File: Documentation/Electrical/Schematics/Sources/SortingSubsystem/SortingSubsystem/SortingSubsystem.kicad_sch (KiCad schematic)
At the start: 5 parts

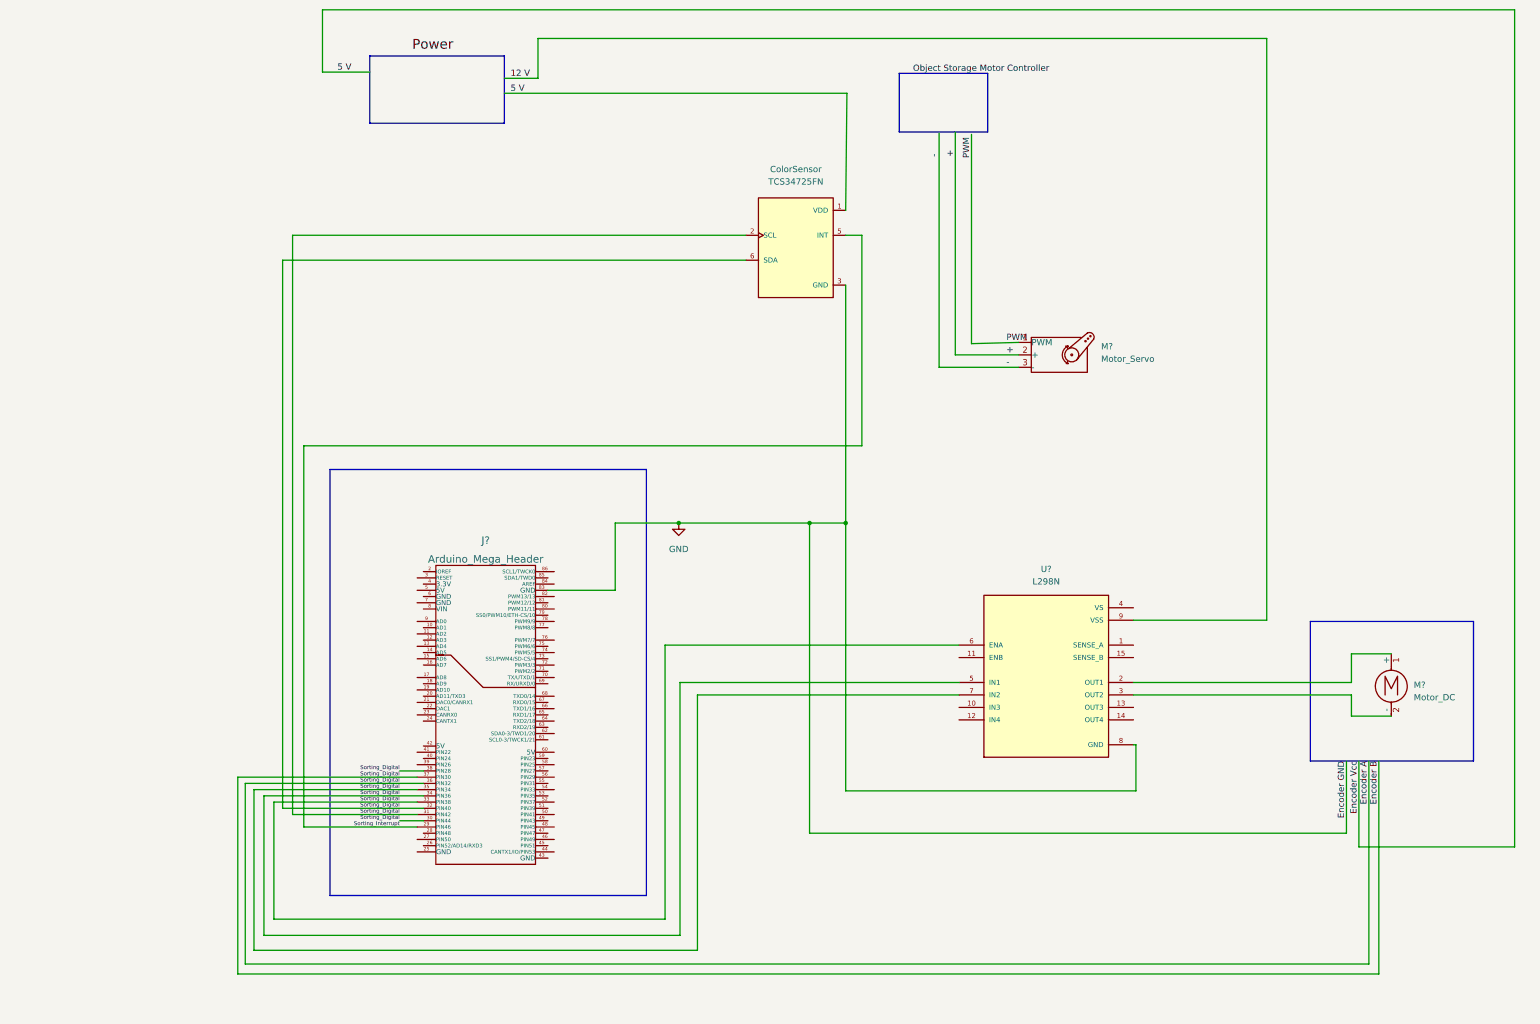
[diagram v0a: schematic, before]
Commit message: added schematic file
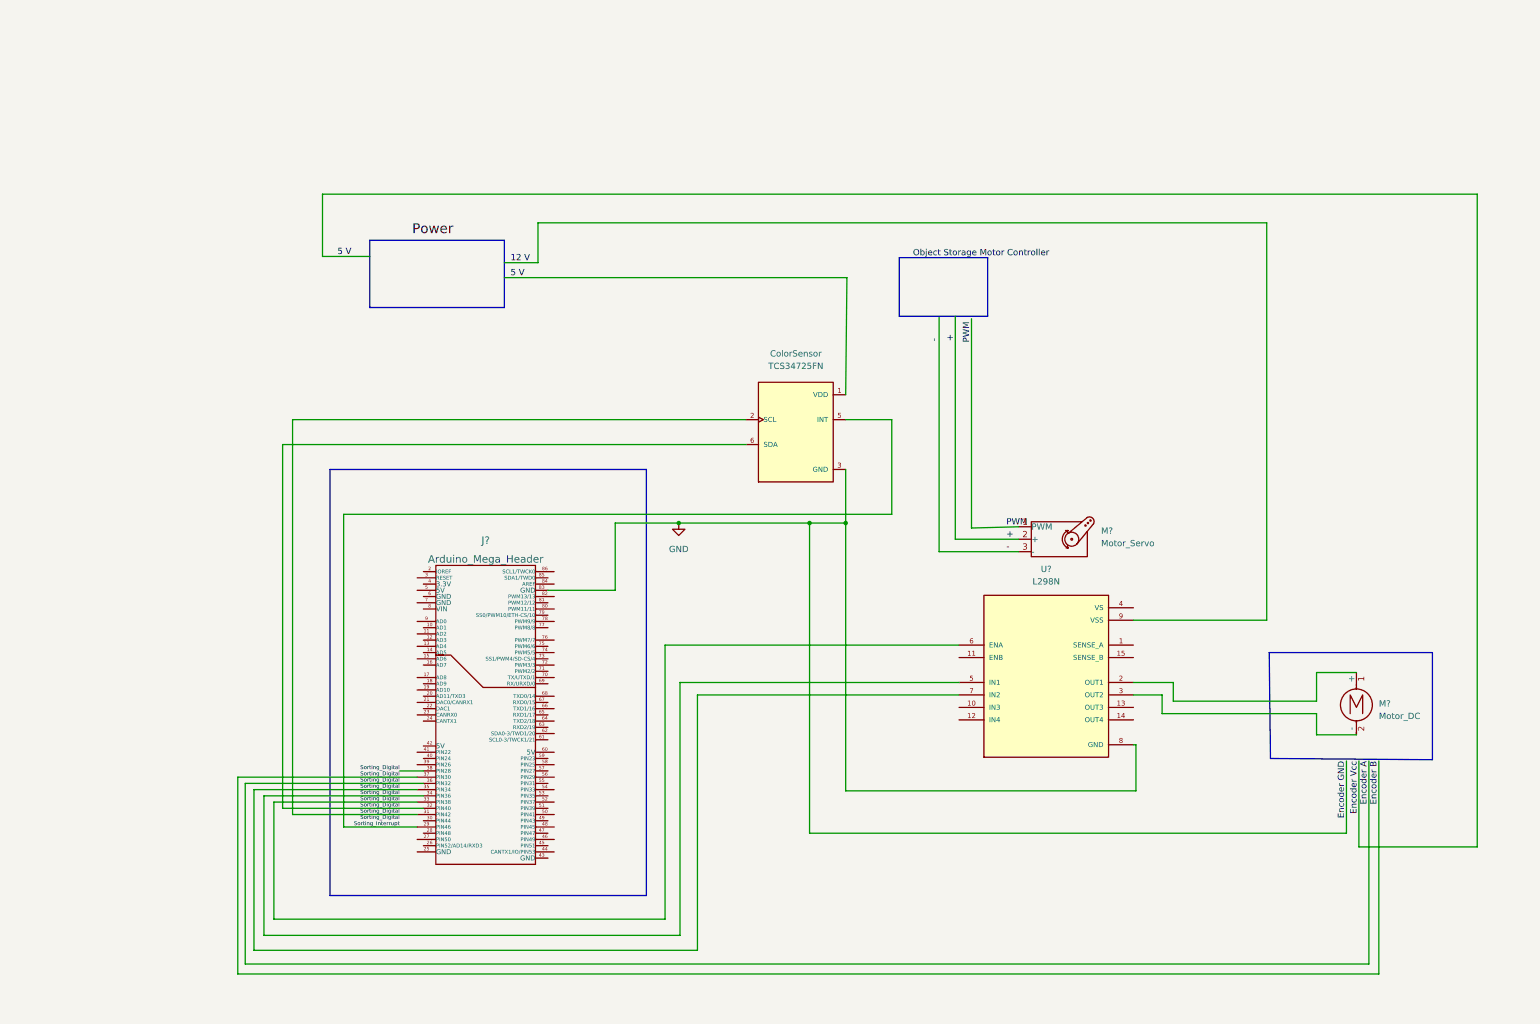
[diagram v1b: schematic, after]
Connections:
- net Encoder A: no longer J?.30 (PIN44)
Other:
- moved on the sheet: ColorSensor, M?

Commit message: schematic update
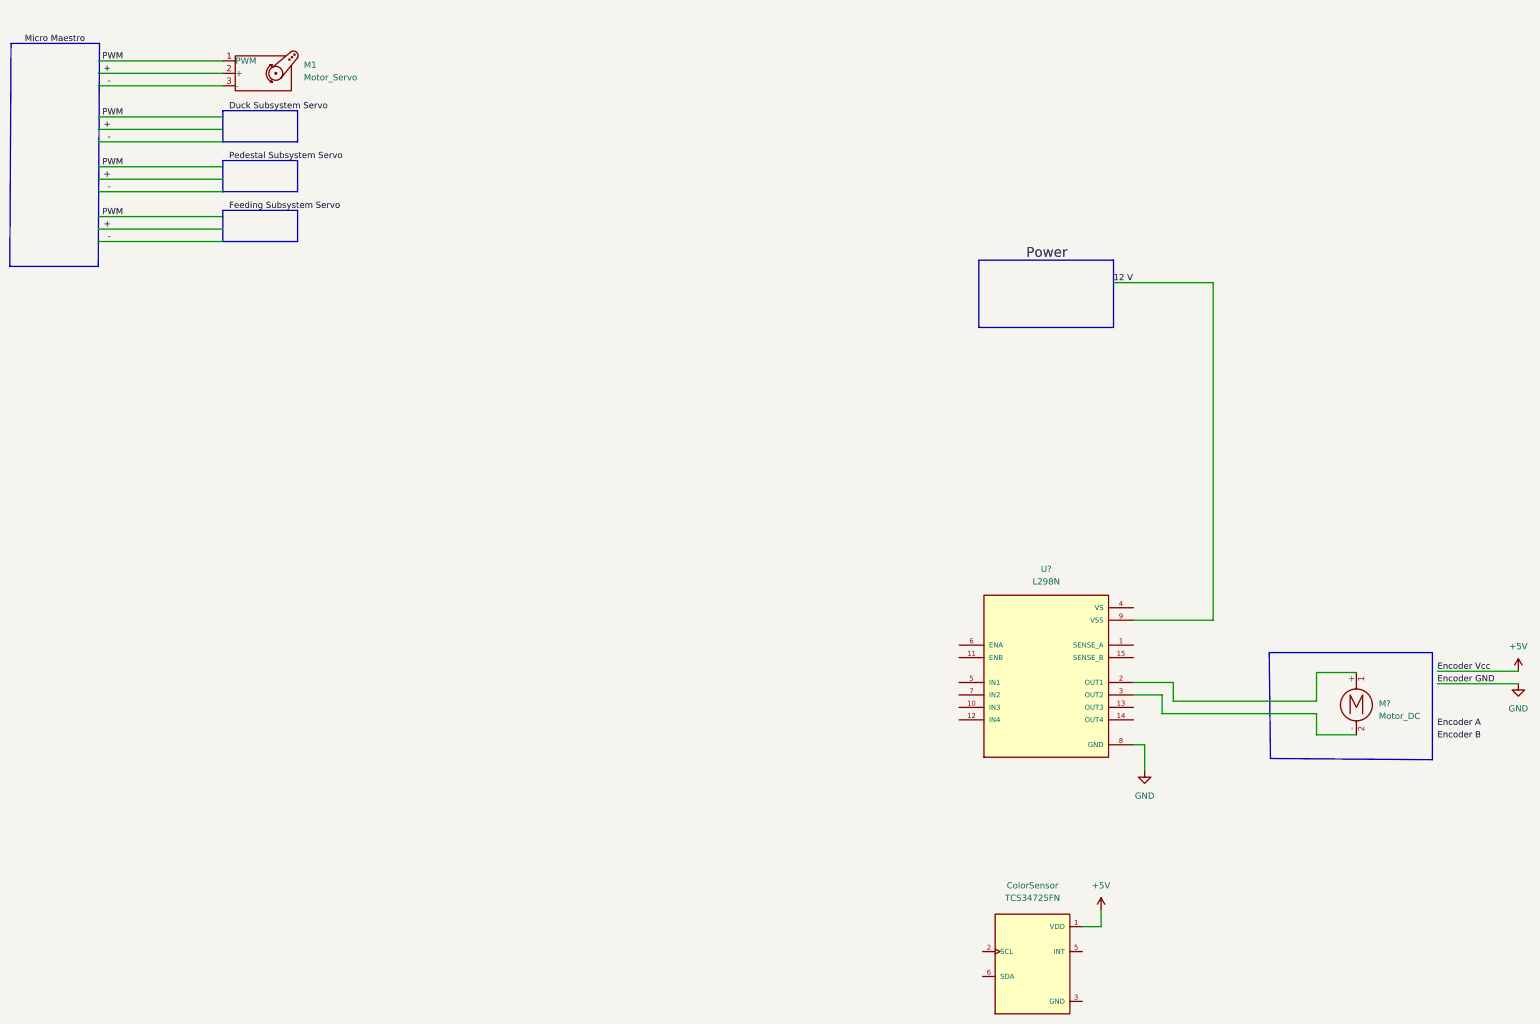
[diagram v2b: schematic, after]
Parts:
- removed J?: Arduino_Mega_Header, symbol w_connectors:Arduino_Mega_Header
- gave numbers to parts that had none: 1
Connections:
- net Encoder A: no longer ColorSensor.2 (SCL), ColorSensor.6 (SDA), U?.5 (IN1), U?.6 (ENA), U?.7 (IN2)
- net GND: no longer ColorSensor.3 (GND)
- net 5 V renamed +5V
- net Sorting_Interrupt: no longer names the net of ColorSensor.5 (INT)
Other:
- moved on the sheet: ColorSensor, M1
